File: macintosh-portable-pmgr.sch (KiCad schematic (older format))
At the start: 5 parts

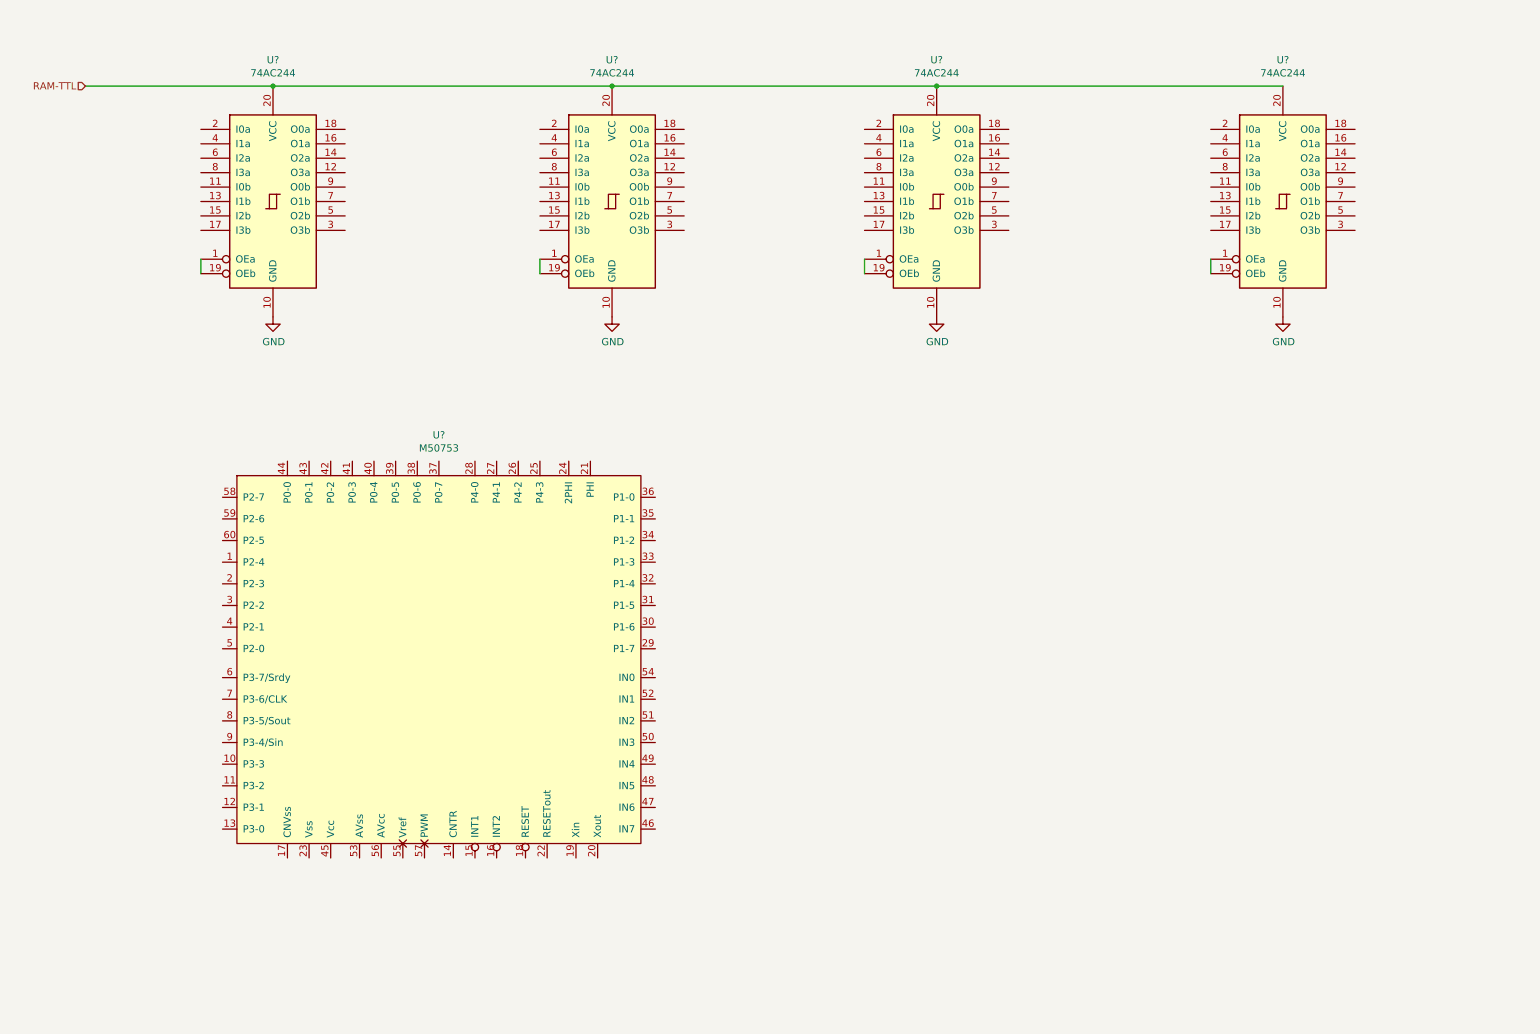
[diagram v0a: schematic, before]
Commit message: Progress on PMGR chip
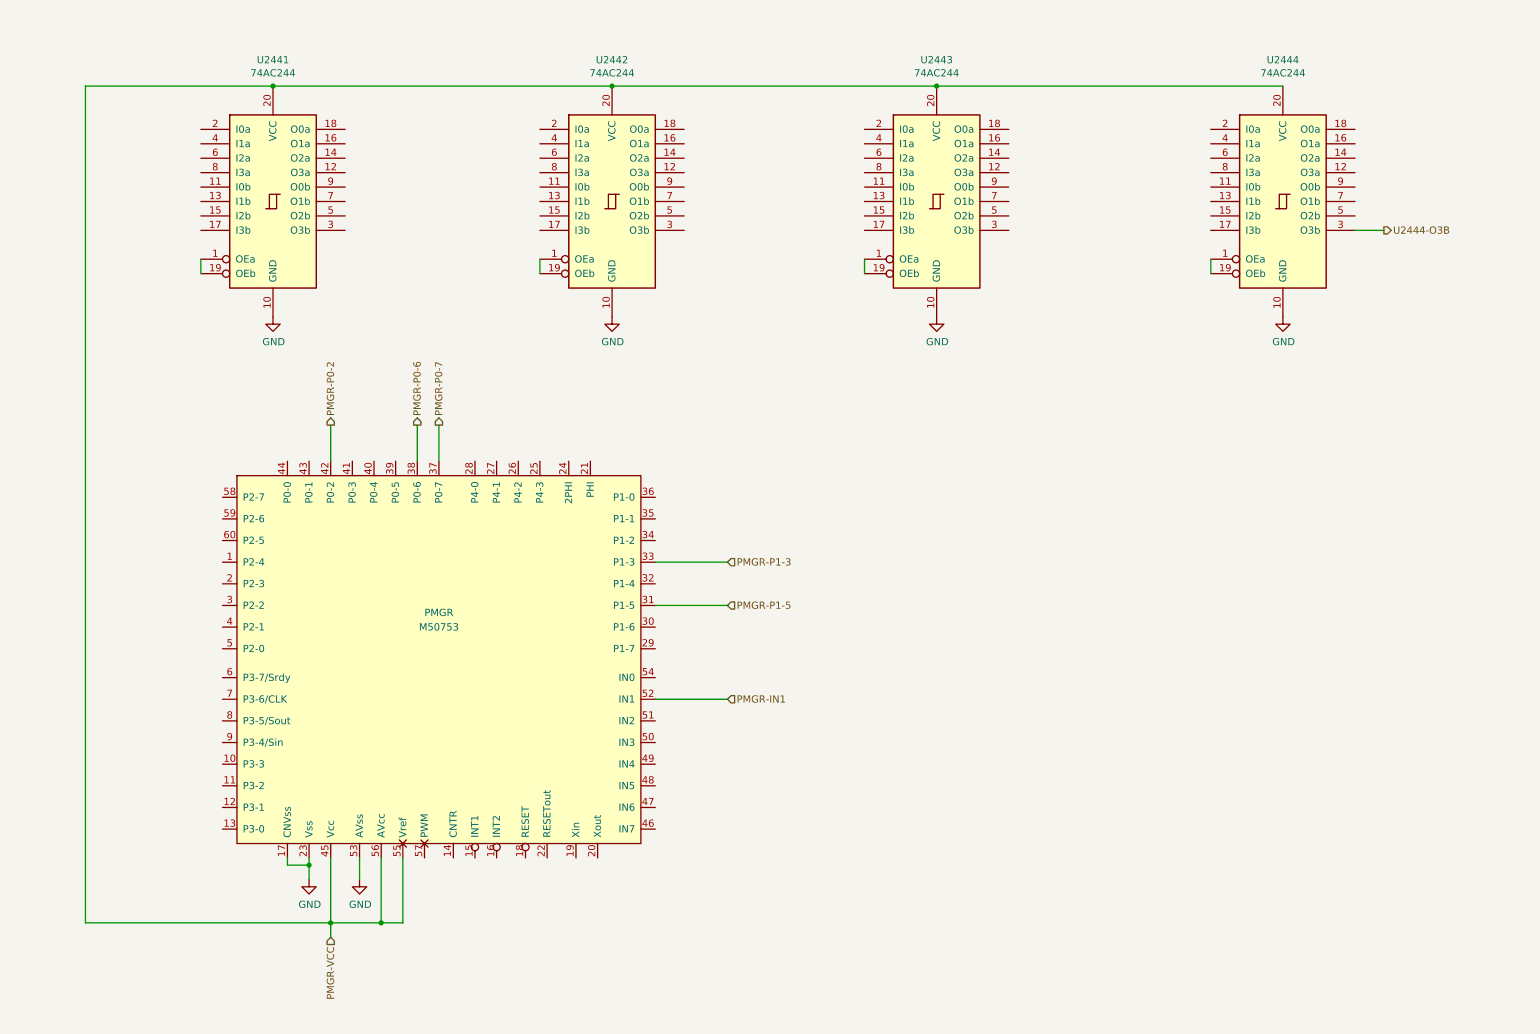
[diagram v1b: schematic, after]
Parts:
- gave numbers to parts that had none: 5
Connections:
- net RAM-TTL is gone; now on net PMGR-VCC: U2441.20 (VCC), U2442.20 (VCC), U2443.20 (VCC), U2444.20 (VCC)
- net GND: now also PMGR.17 (CNVss), PMGR.23 (Vss), PMGR.53 (AVss)
- net PMGR-P1-5: now reaches PMGR.31 (P1-5)
- net PMGR-P1-3: now reaches PMGR.33 (P1-3)
- net PMGR-P0-7: now reaches PMGR.37 (P0-7)
- net PMGR-P0-6: now reaches PMGR.38 (P0-6)
- net PMGR-P0-2: now reaches PMGR.42 (P0-2)
- net PMGR-VCC: now reaches PMGR.45 (Vcc)
- net PMGR-VCC: now also PMGR.55 (Vref), PMGR.56 (AVcc)
- net PMGR-IN1: now reaches PMGR.52 (IN1)
- net U2444-O3B: now reaches U2444.3 (O3b)
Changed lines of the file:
@@
 $Descr A4 11693 8268
 encoding utf-8
-Sheet 5 5
+Sheet 4 5
 Title ""
-Date ""
-Rev ""
-Comp ""
-Comment1 ""
+Date "2019-06-08"
+Rev "0.13"
+Comp "https://oldcrap.org"
+Comment1 "Author: Pawel Pieczul"
 Comment2 ""
 Comment3 ""
@@
 $EndDescr
 $Comp
-L 74xx:74LS244 U?
+L 74xx:74LS244 U2441
 U 1 1 5D18C1C5
 P 2400 2050
-F 0 "U?" H 2400 3031 50  0000 C CNN
+F 0 "U2441" H 2400 3031 50  0000 C CNN
 F 1 "74AC244" H 2400 2940 50  0000 C CNN
 F 2 "" H 2400 2050 50  0001 C CNN
@@
 $EndComp
 $Comp
-L 74xx:74LS244 U?
+L 74xx:74LS244 U2443
 U 1 1 5D18EE70
 P 7000 2050
-F 0 "U?" H 7000 3031 50  0000 C CNN
+F 0 "U2443" H 7000 3031 50  0000 C CNN
 F 1 "74AC244" H 7000 2940 50  0000 C CNN
 F 2 "" H 7000 2050 50  0001 C CNN
@@
 $EndComp
 $Comp
-L 74xx:74LS244 U?
+L 74xx:74LS244 U2444
 U 1 1 5D18F8CC
 P 9400 2050
-F 0 "U?" H 9400 3031 50  0000 C CNN
+F 0 "U2444" H 9400 3031 50  0000 C CNN
 F 1 "74AC244" H 9400 2940 50  0000 C CNN
 F 2 "" H 9400 2050 50  0001 C CNN
@@
 $EndComp
 $Comp
-L 74xx:74LS244 U?
+L 74xx:74LS244 U2442
 U 1 1 5D1B6555
 P 4750 2050
-F 0 "U?" H 4750 3031 50  0000 C CNN
+F 0 "U2442" H 4750 3031 50  0000 C CNN
 F 1 "74AC244" H 4750 2940 50  0000 C CNN
 F 2 "" H 4750 2050 50  0001 C CNN
@@
 	1    0    0    -1
 $EndComp
-Text HLabel 1100 1250 0    50   Input ~ 0
-RAM-TTL
 Wire Wire Line
 	1100 1250 2400 1250
@@
 	1900 2450 1900 2550
 $Comp
-L macintosh-portable:M50753 U?
+L macintosh-portable:M50753 PMGR
 U 1 1 5CF2D32E
 P 3550 5200
-F 0 "U?" H 3550 6731 50  0000 C CNN
-F 1 "M50753" H 3550 6640 50  0000 C CNN
+F 0 "PMGR" H 3550 5500 50  0000 C CNN
+F 1 "M50753" H 3550 5400 50  0000 C CNN
 F 2 "" H 3700 5150 50  0001 C CNN
 F 3 "" H 3700 5150 50  0001 C CNN
@@
 	1    0    0    -1
 $EndComp
+Text HLabel 5550 4550 2    50   Input ~ 0
+PMGR-P1-3
+Wire Wire Line
+	5050 4550 5550 4550
+Text HLabel 3550 3600 1    50   Output ~ 0
+PMGR-P0-7
+Wire Wire Line
+	3550 3600 3550 3850
+Text HLabel 2800 3600 1    50   Output ~ 0
+PMGR-P0-2
+Wire Wire Line
+	2800 3600 2800 3850
+Text HLabel 2800 7150 3    50   Input ~ 0
+PMGR-VCC
+$Comp
+L power:GND #PWR?
+U 1 1 5CFC9A73
+P 2650 6750
+F 0 "#PWR?" H 2650 6500 50  0001 C CNN
+F 1 "GND" H 2655 6577 50  0000 C CNN
+F 2 "" H 2650 6750 50  0001 C CNN
+F 3 "" H 2650 6750 50  0001 C CNN
+	1    2650 6750
+	1    0    0    -1
+$EndComp
+Wire Wire Line
+	2650 6750 2650 6650
+Wire Wire Line
+	2500 6600 2500 6650
+Wire Wire Line
+	2500 6650 2650 6650
+Connection ~ 2650 6650
+Wire Wire Line
+	2650 6650 2650 6600
+$Comp
+L power:GND #PWR?
+U 1 1 5CFCB83B
+P 3000 6750
+F 0 "#PWR?" H 3000 6500 50  0001 C CNN
+F 1 "GND" H 3005 6577 50  0000 C CNN
+F 2 "" H 3000 6750 50  0001 C CNN
+F 3 "" H 3000 6750 50  0001 C CNN
+	1    3000 6750
+	1    0    0    -1
+$EndComp
+Wire Wire Line
+	3000 6600 3000 6750
+Wire Wire Line
+	2800 6600 2800 7050
+Wire Wire Line
+	2800 7050 3150 7050
+Wire Wire Line
+	3150 7050 3150 6600
+Connection ~ 2800 7050
+Wire Wire Line
+	2800 7050 2800 7150
+Wire Wire Line
+	3150 7050 3300 7050
+Wire Wire Line
+	3300 7050 3300 6600
+Connection ~ 3150 7050
+Text HLabel 5550 5500 2    50   Input ~ 0
+PMGR-IN1
+Wire Wire Line
+	5550 5500 5050 5500
+Text HLabel 3400 3600 1    50   Output ~ 0
+PMGR-P0-6
+Wire Wire Line
+	3400 3600 3400 3850
+Text HLabel 10100 2250 2    50   Output ~ 0
+U2444-O3B
+Wire Wire Line
+	9900 2250 10100 2250
+Text HLabel 5550 4850 2    50   Input ~ 0
+PMGR-P1-5
+Wire Wire Line
+	5550 4850 5050 4850
+Wire Wire Line
+	1100 1250 1100 7050
+Wire Wire Line
+	1100 7050 2800 7050
 $EndSCHEMATC

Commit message: Added reset circuit.
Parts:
- added C15, C24: 1uF, symbol Device:CP1
- added R132: 1k, symbol Device:R_US
- added R143, R155, R156: 10k, symbol Device:R_US
- added R144: 100k, symbol Device:R_US
- added S2: NMI, symbol Switch:SW_Push
- added S3: RESET, symbol Switch:SW_Push
- added U7402: 74AC02, symbol 74xx_IEEE:7402
- added U7410: 74AC10, symbol 74xx_IEEE:7410
- added U74153: 74AC153, symbol 74xx_IEEE:74153
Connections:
- net labels added: CPU-ROM-VCC, HALT, MISC-GLU-6, RESET
- wire segments 28 -> 85
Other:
- note added: "CPU"
- note added: "CPU, VIA"
- note added: "VIA & ASC chips"
- moved on the sheet: U2441, U2442, U2443, U2444

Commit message: More progress on PMGR chip
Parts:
- removed U2441, U2442, U2443, U2444: 74AC244, symbol 74xx:74LS244
- removed U7402: 74AC02, symbol 74xx_IEEE:7402
- removed U7410: 74AC10, symbol 74xx_IEEE:7410
- removed U74153: 74AC153, symbol 74xx_IEEE:74153
- added C14: 10uF, symbol Device:C
- added Q18: U92, symbol Device:Q_NPN_BCE
- added Q19: P2A, symbol Device:Q_PNP_BCE
- added R152: 10k, symbol Device:R_US
- added R153: 100k, symbol Device:R_US
- added SW1: DTS-4, symbol Switch:SW_DIP_x04
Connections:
- net labels added: CPU-GLU-56, DISPLAY-26, MISC-GLU-27, PMGR-IN3, VIA-CA2, VIA-CB1, VIA-PA0, VIA-PA1, VIA-PA2, VIA-PA3, VIA-PA4, VIA-PA5, VIA-PA6, VIA-PA7, VIA-PB0, VIA-PB1, VIA-PB2
- net labels removed: U2444-O3B
- wire segments 85 -> 100
- no-connect marks 0 -> 2
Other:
- note added: "J19 connector\nDisplay contrast"
- note added: "Modem pin 17"
- note added: "To blank R17"
- note removed: "VIA & ASC chips"
- moved on the sheet: C15, C24
